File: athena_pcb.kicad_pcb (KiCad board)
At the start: 2 copper layers, 32 parts, among them J1 Conn_02x03_Odd_Even, SW1 SW_Push, SW2 SW_Push, U1 NRF5340-QKAA-R7, U2 BME280, Y1 32MHz, Y2 32.768kHz

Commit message: Added board layout constraints
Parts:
- moved BT1 29.3 mm to (114.3, 71.1)
- moved U1 5.00 mm to (116.0, 90.7)
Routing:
- net VDD: track 0.00 -> 7.67 mm
- net GND: track 0.00 -> 2.51 mm
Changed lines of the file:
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@@
   (layers
     (0 "F.Cu" signal)
-    (31 "B.Cu" signal)
+    (31 "B.Cu" power)
     (32 "B.Adhes" user "B.Adhesive")
     (33 "F.Adhes" user "F.Adhesive")
@@
   )
   (setup
+    (stackup
+      (layer "F.SilkS" (type "Top Silk Screen"))
+      (layer "F.Paste" (type "Top Solder Paste"))
+      (layer "F.Mask" (type "Top Solder Mask") (thickness 0.01))
+      (layer "F.Cu" (type "copper") (thickness 0.035))
+      (layer "dielectric 1" (type "core") (thickness 1.51) (material "FR4") (epsilon_r 4.5) (loss_tangent 0.02))
+      (layer "B.Cu" (type "copper") (thickness 0.035))
+      (layer "B.Mask" (type "Bottom Solder Mask") (thickness 0.01))
+      (layer "B.Paste" (type "Bottom Solder Paste"))
+      (layer "B.SilkS" (type "Bottom Silk Screen"))
+      (copper_finish "None")
+      (dielectric_constraints no)
+    )
     (pad_to_mask_clearance 0)
     (pcbplotparams
@@
   (net 83 "unconnected-(U1C-P0.27{slash}AIN6-PadAK30)")
   (footprint "NRF5340-QKAA-R7:XCVR_NRF5340-QKAA-R7" (layer "F.Cu")
-    (at 116.18 85.7)
+    (at 115.973 90.7)
     (property "MANUFACTURER" "Nordic Semiconductor")
     (property "MAXIMUM_PACKAGE_HEIGHT" "0.85mm")
@@
   )
   (footprint "Battery:BatteryHolder_Keystone_1060_1x2032" (layer "F.Cu")
-    (at 142.41 79.220467)
+    (at 114.3 71.12)
     (descr "http://www.keyelco.com/product-pdf.cfm?p=726")
     (tags "CR2032 BR2032 BatteryHolder Battery")
@@
     )
   )
+  (segment (start 131.72 91.08) (end 131.72 91.44) (width 0.3) (layer "F.Cu") (net 1))
+  (segment (start 129.54 88.9) (end 131.72 91.08) (width 0.3) (layer "F.Cu") (net 1))
+  (segment (start 128.877035 88.9) (end 129.54 88.9) (width 0.3) (layer "F.Cu") (net 1))
+  (segment (start 126.39 91.387035) (end 128.877035 88.9) (width 0.3) (layer "F.Cu") (net 1))
+  (segment (start 126.39 91.43) (end 126.39 91.387035) (width 0.3) (layer "F.Cu") (net 1))
+  (segment (start 132.3 91.32) (end 132.3 89.12) (width 0.3) (layer "F.Cu") (net 2))
+  (segment (start 132.3 89.12) (end 132.08 88.9) (width 0.3) (layer "F.Cu") (net 2))
 )

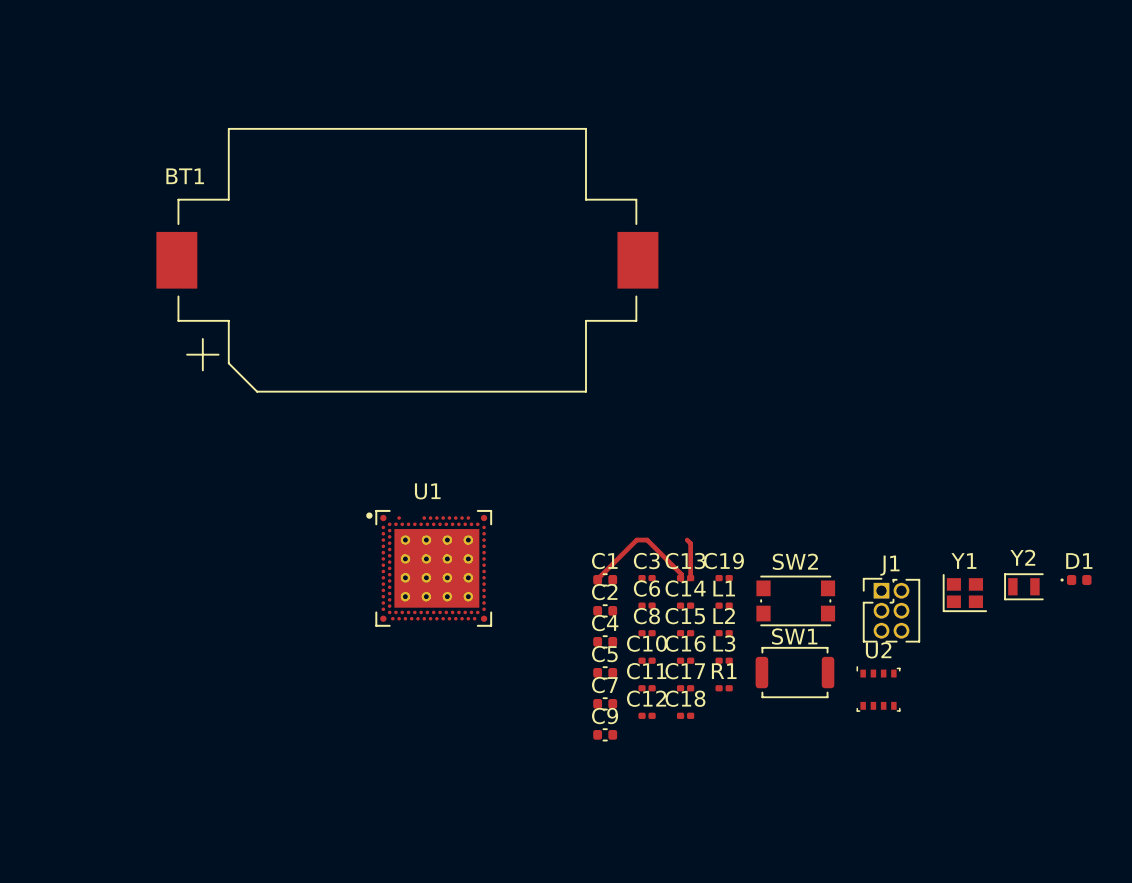
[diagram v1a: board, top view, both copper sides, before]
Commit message: Layout around NRF53 done
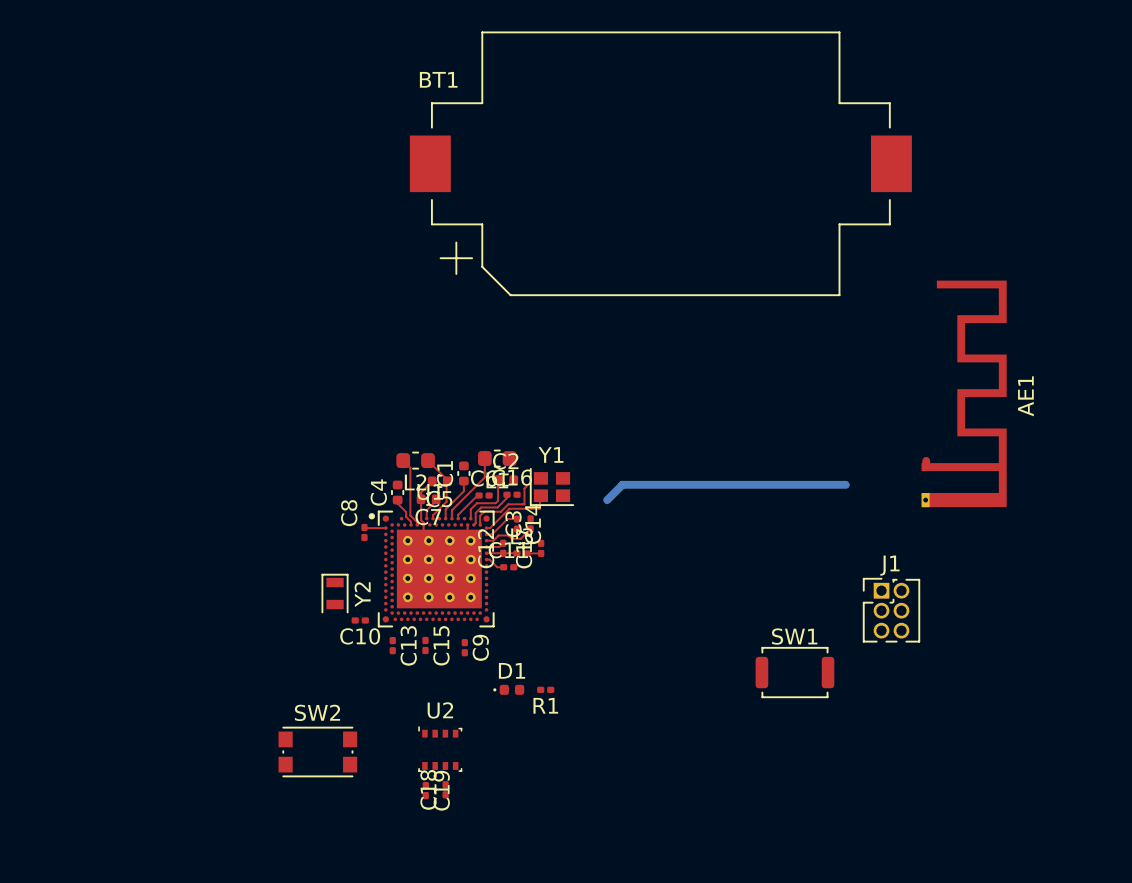
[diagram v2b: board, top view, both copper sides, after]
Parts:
- added AE1: Antenna, RF_Antenna:Texas_SWRA117D_2.4GHz_Left, F.Cu at (147.2, 84.3)
- C9: footprint Capacitor_SMD:C_0402_1005Metric -> Capacitor_SMD:C_0201_0603Metric
- L1, L2: footprint Inductor_SMD:L_0201_0603Metric -> Inductor_SMD:L_0603_1608Metric
- moved Y2 43.8 mm to (109.7, 92.3), turned to -90 degrees
- moved D1 36.7 mm to (120.9, 98.4)
- moved SW2 31.9 mm to (108.6, 102.4)
- moved U2 28.1 mm to (116.4, 102.2)
- moved Y1 27.1 mm to (123.5, 85.5)
- moved C19 23.3 mm to (115.5, 104.8), turned to -90 degrees
- moved L2 22.5 mm to (114.8, 83.8), turned to 180 degrees
- moved C13 19.1 mm to (113.4, 95.6), turned to -90 degrees
- moved C8 19.1 mm to (111.6, 88.4), turned to -90 degrees
- moved C10 18.4 mm to (111.3, 94.0), turned to 180 degrees
- moved BT1 17.2 mm to (130.4, 65.0)
- moved L1 17.2 mm to (120.0, 83.7), turned to 180 degrees
- moved C7 17.2 mm to (115.7, 86.3), turned to 180 degrees
- moved C15 16.5 mm to (115.5, 95.6), turned to -90 degrees
- moved C4 16.2 mm to (113.7, 85.9), turned to 90 degrees
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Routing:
- net (no net): track 0.00 -> 15.6 mm
- net GND: track 2.51 -> 11.0 mm
- net Net-(U1A-DECR): track 0.00 -> 6.98 mm
- net VDD: track 7.67 -> 13.2 mm
- net Net-(U1B-XC2): track 0.00 -> 4.90 mm
- net Net-(U1A-DCC): track 0.00 -> 4.85 mm
- net Net-(U1B-XC1): track 0.00 -> 4.76 mm
- net Net-(U1A-DECD): track 0.00 -> 4.58 mm
- net Net-(U1A-DCCD): track 0.00 -> 4.46 mm
- net Net-(U1A-DECN): track 0.00 -> 2.02 mm
- net Net-(U1B-ANT): track 0.00 -> 1.93 mm
- net Net-(U1A-DECA): track 0.00 -> 1.52 mm
- net Net-(AE1-A): track 0.00 -> 1.26 mm

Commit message: Added new 0201 capacitor footprint
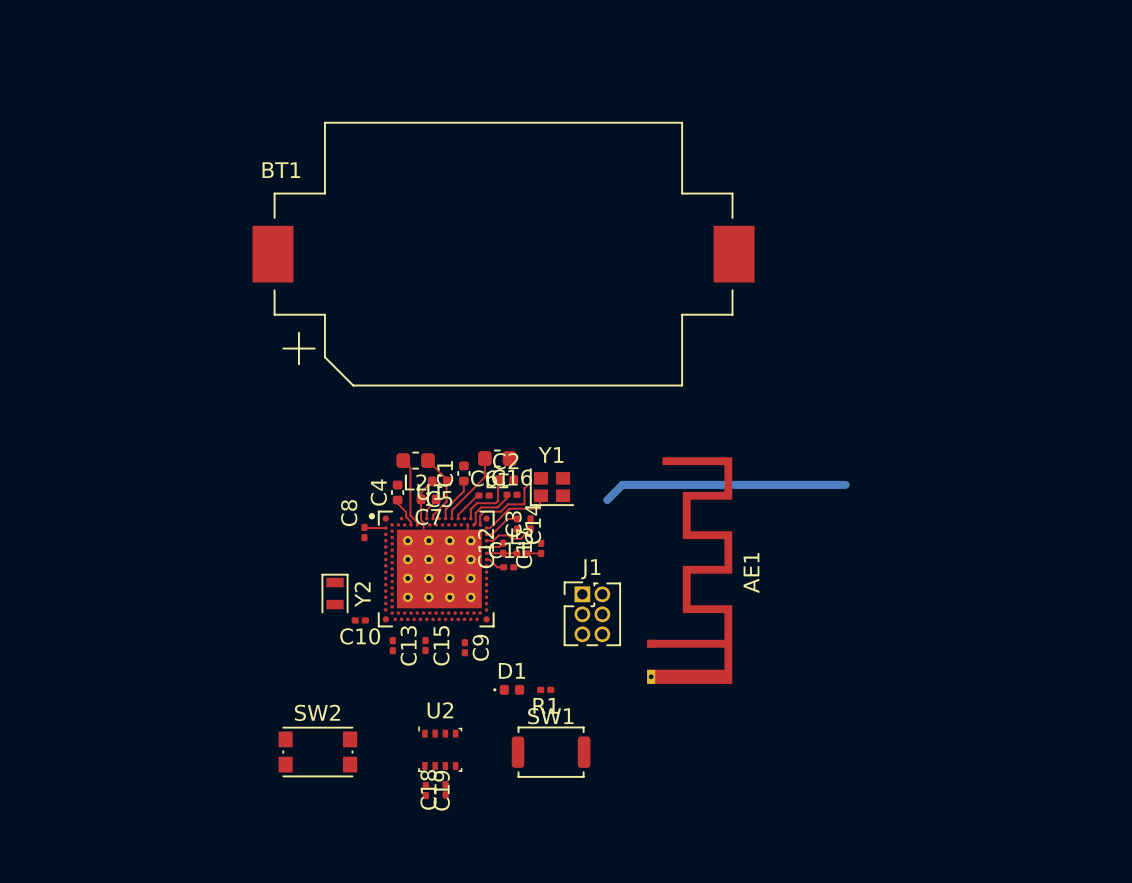
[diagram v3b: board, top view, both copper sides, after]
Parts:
- moved AE1 20.7 mm to (129.8, 95.5)
- moved J1 19.0 mm to (125.4, 92.3)
- moved SW1 16.3 mm to (123.4, 102.4)
- moved BT1 11.5 mm to (120.4, 70.7)
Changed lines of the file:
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@@
   )
   (footprint "Connector_PinHeader_1.27mm:PinHeader_2x03_P1.27mm_Vertical" (layer "F.Cu")
-    (at 144.43 92.12)
+    (at 125.42 92.35)
     (descr "Through hole straight pin header, 2x03, 1.27mm pitch, double rows")
     (tags "Through hole pin header THT 2x03 1.27mm double row")
@@
   )
   (footprint "Battery:BatteryHolder_Keystone_1060_1x2032" (layer "F.Cu")
-    (at 130.41 64.99)
+    (at 120.41 70.73)
     (descr "http://www.keyelco.com/product-pdf.cfm?p=726")
     (tags "CR2032 BR2032 BatteryHolder Battery")
@@
   )
   (footprint "Button_Switch_SMD:SW_Push_SPST_NO_Alps_SKRK" (layer "F.Cu")
-    (at 138.93 97.32)
+    (at 123.43 102.38)
     (descr "http://www.alps.com/prod/info/E/HTML/Tact/SurfaceMount/SKRK/SKRKAHE020.html")
     (tags "SMD SMT button")
@@
   )
   (footprint "RF_Antenna:Texas_SWRA117D_2.4GHz_Left" (layer "F.Cu")
-    (at 147.235 84.26 -90)
+    (at 129.795 95.49 -90)
     (descr "http://www.ti.com/lit/an/swra117d/swra117d.pdf")
     (tags "PCB antenna")
@@
   (segment (start 120.39 89.74) (end 121.25 89.74) (width 0.127) (layer "F.Cu") (net 7))
   (segment (start 119.33 89.74) (end 120.39 89.74) (width 0.127) (layer "F.Cu") (net 7))
-  (segment (start 147.27 84.23) (end 147.27 83.87) (width 0.5) (layer "F.Cu") (net 8))
   (segment (start 121.9 89.75) (end 122.8 89.75) (width 0.127) (layer "F.Cu") (net 8))
   (segment (start 119.2225 83.72) (end 119.335 83.8325) (width 0.127) (layer "F.Cu") (net 15))

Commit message: Added board outline
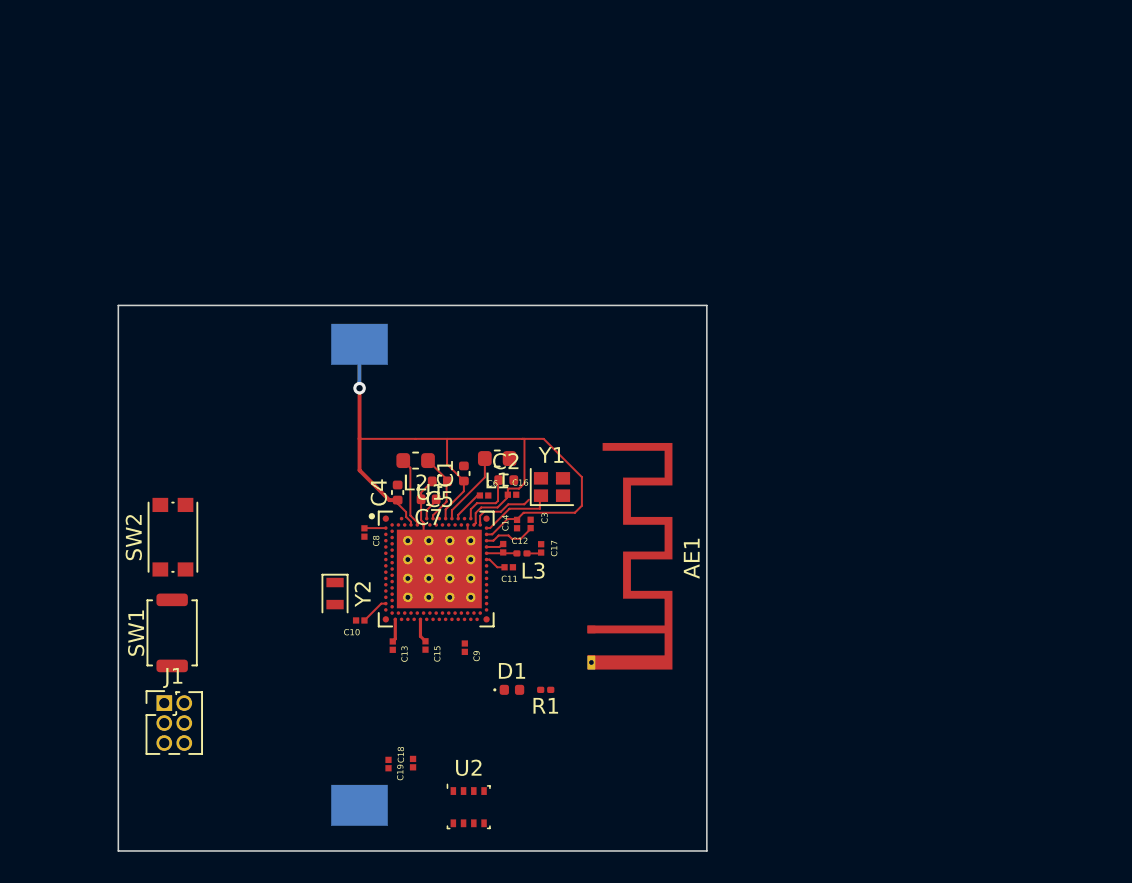
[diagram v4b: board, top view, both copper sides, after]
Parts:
- BT1: moved to B.Cu
- C10, C11, C12, C13, C14, C15, C16, C17, C18, C19, C3, C6, C8, C9: footprint Capacitor_SMD:C_0201_0603Metric -> GRM033R71C301JA01D:CAPC0603X33N
- moved J1 27.5 mm to (98.8, 99.3)
- moved SW1 25.2 mm to (99.3, 94.8), turned to 90 degrees
- moved BT1 22.3 mm to (111.3, 91.1), turned to -90 degrees
- moved SW2 16.5 mm to (99.4, 88.7), turned to 90 degrees
- moved U2 4.07 mm to (118.2, 105.9)
- moved AE1 3.91 mm to (126.0, 94.6)
- moved C19 2.91 mm to (113.1, 103.1)
- moved C18 2.67 mm to (114.7, 103.1)
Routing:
- net VDD: track 13.2 -> 58.4 mm, vias 0 -> 1
- net (no net): track 15.6 -> 0.00 mm
- net Net-(U1B-XC2): track 4.90 -> 4.11 mm
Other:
- board outline added: 37.4 x 34.7 mm

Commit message: Added testpoints
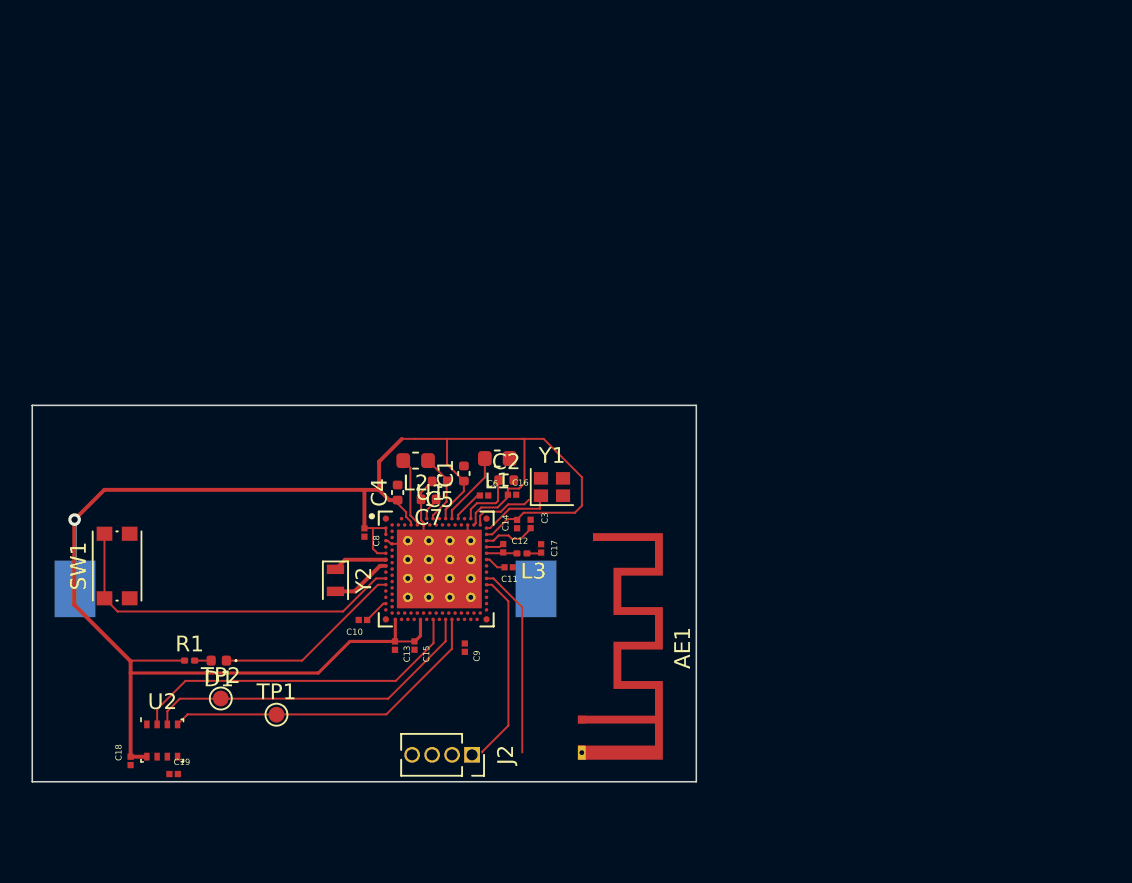
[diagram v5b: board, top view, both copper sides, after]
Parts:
- removed J1: Conn_02x03_Odd_Even, Connector_PinHeader_1.27mm:PinHeader_2x03_P1.27mm_Vertical
- removed the SW1 at (99.3, 94.8)
- added J2: Conn_01x04, Connector_PinSocket_1.27mm:PinSocket_1x04_P1.27mm_Vertical, F.Cu at (118.4, 102.5)
- added TP1: TestPoint, TestPoint:TestPoint_Pad_D1.0mm, F.Cu at (106.0, 100.0)
- added TP2: TestPoint, TestPoint:TestPoint_Pad_D1.0mm, F.Cu at (102.4, 99.0)
- moved R1 22.7 mm to (100.5, 96.6), turned to 0 degrees
- moved U2 19.9 mm to (98.7, 101.6)
- moved D1 18.7 mm to (102.3, 96.6), turned to 180 degrees
- moved C18 18.0 mm to (96.7, 102.9)
- moved C19 13.7 mm to (99.4, 103.8), turned to 0 degrees
- moved AE1 5.76 mm to (125.4, 100.3)
- moved SW1 3.99 mm to (95.8, 90.5)
- moved BT1 3.54 mm to (107.8, 92.0), turned to 0 degrees
- moved Y2 0.84 mm to (109.7, 91.5)
- moved C15 0.70 mm to (114.8, 95.6)
- moved C10 0.17 mm to (111.5, 94.0)
- moved C13 0.14 mm to (113.5, 95.6)
- renumbered SW2 to SW1
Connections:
- D1 pad 1: /P0.24 -> /P0.03
- SW1 pad 1: /P0.23 -> /P0.02
- U1 pad AA1: unconnected-(U1C-P0.03/NFC2-PadAA1) -> /P0.03
- U1 pad AL13: unconnected-(U1C-P0.19-PadAL13) -> /SDO
- U1 pad AL15: unconnected-(U1C-P0.21-PadAL15) -> /CSB
- U1 pad AL19: unconnected-(U1D-P1.04-PadAL19) -> /SDI_SDA
- U1 pad AL21: unconnected-(U1D-P1.06-PadAL21) -> /SCK_SCL
- U1 pad W1: unconnected-(U1C-P0.02/NFC1-PadW1) -> /P0.02
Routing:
- net VDD: track 58.4 -> 117.6 mm
- net /P0.02: track 0.00 -> 23.2 mm
- net /CSB: track 0.00 -> 21.8 mm
- net /SDI_SDA: track 0.00 -> 21.8 mm
- net /SCK_SCL: track 0.00 -> 21.3 mm
- net /SWDCLK: track 0.00 -> 12.3 mm
- net /P0.03: track 0.00 -> 12.1 mm
- net /SWDIO: track 0.00 -> 12.1 mm
- net Net-(U1C-P0.01/XL2): track 0.00 -> 3.87 mm
- net Net-(U1C-P0.00/XL1): track 0.00 -> 3.50 mm
- net GND: track 11.0 -> 12.6 mm
- net Net-(D1-A): track 0.00 -> 1.05 mm
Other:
- board size 37.4 x 34.7 mm -> 42.2 x 23.9 mm
